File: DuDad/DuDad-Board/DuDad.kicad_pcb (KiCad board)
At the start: 2 copper layers, 60.6 x 24 mm, 24 parts, among them J1 EXP, J2 USB_B_Micro, J3 USB_A, Q1 2N3906, Q2 2N3906, Q3 2N7000, Q4 2N3906, SW1 Reset

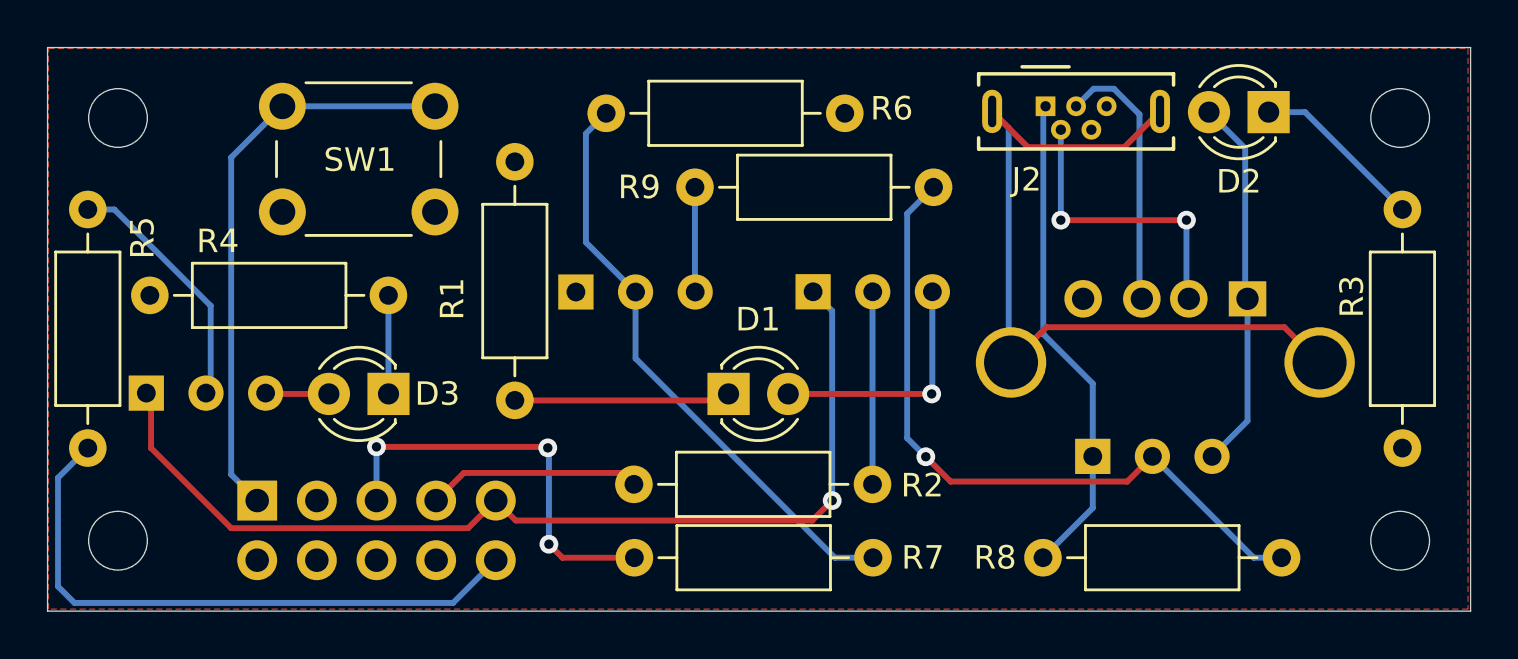
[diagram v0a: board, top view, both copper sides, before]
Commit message: Adds 2HP DuDad
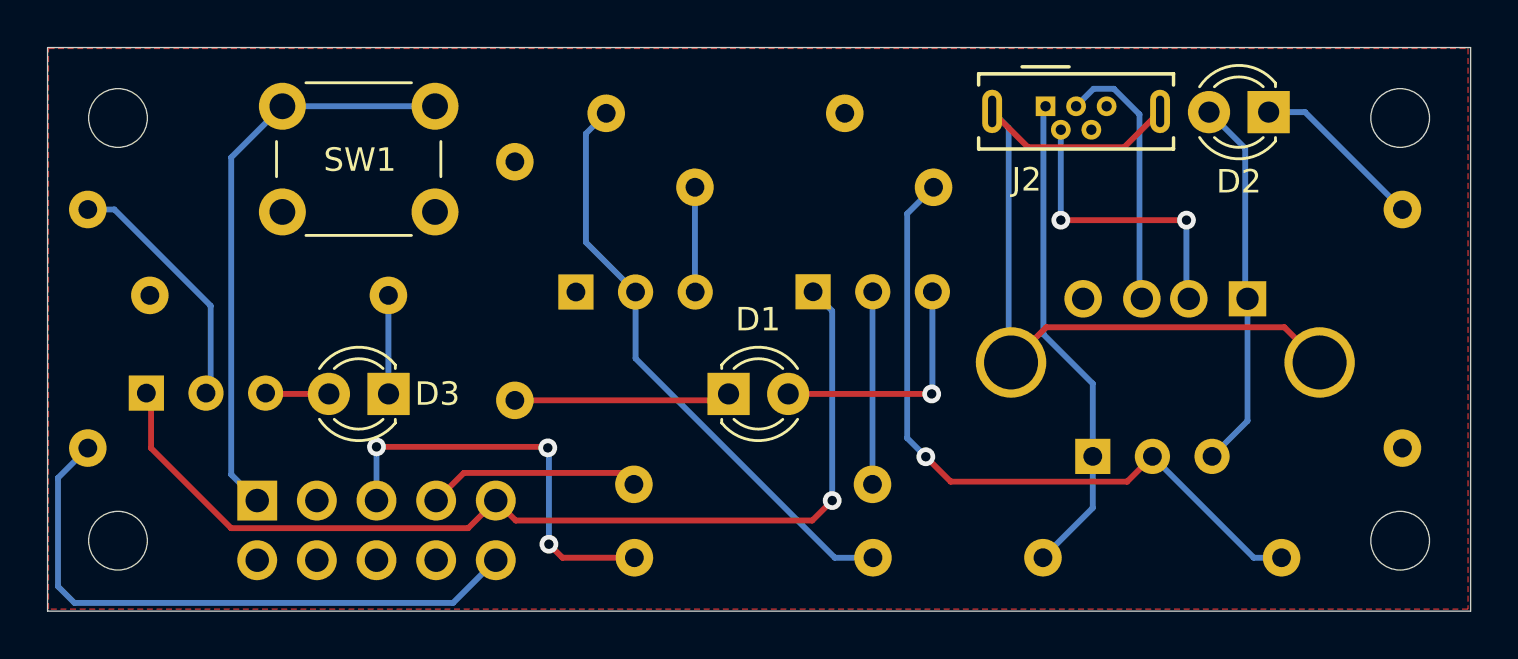
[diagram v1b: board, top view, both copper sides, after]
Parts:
- R1, R2, R3, R4, R5, R6, R7, R8, R9: moved to B.Cu
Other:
- board text added: "DuDad"
- board text added: "v1.4"
- board text removed: "DuDad v 1.3"

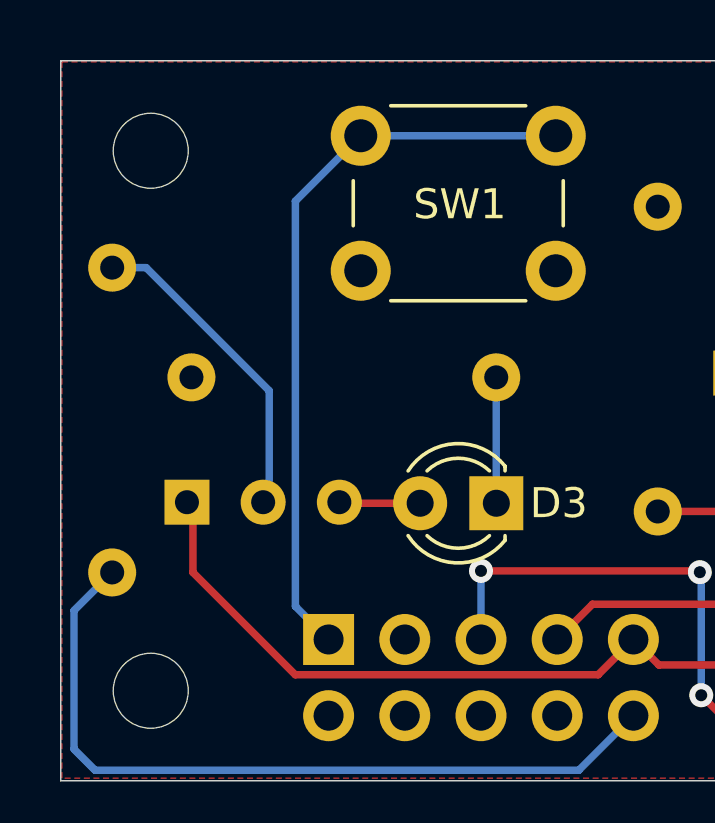
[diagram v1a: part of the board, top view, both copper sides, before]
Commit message: Ups resistor values to dim LEDs. Adds generate BOMs.
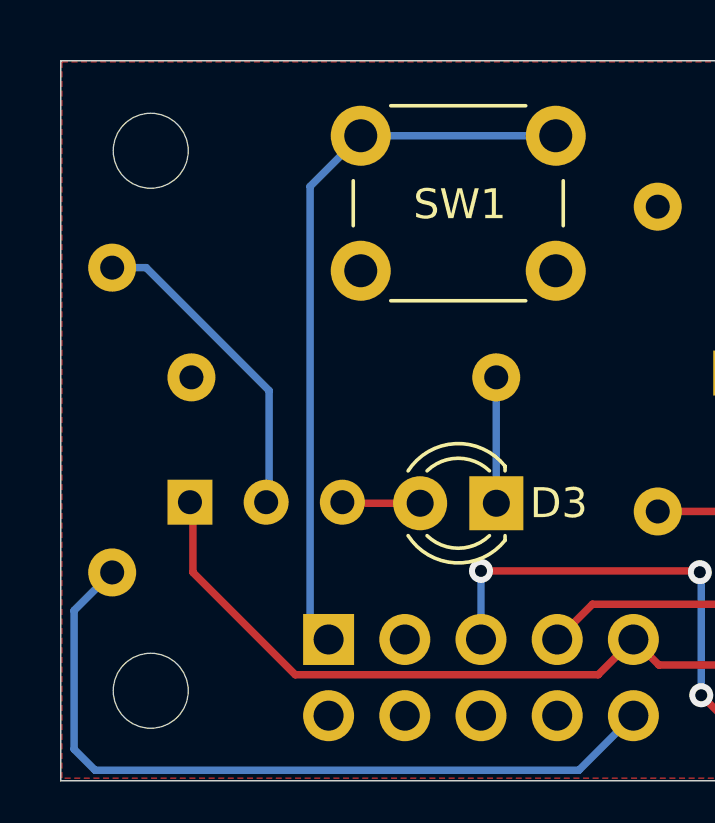
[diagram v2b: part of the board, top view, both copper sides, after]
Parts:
- R1, R4: value 200 -> 620
- R2, R5, R7, R8: value 43K -> 30K
- moved Q2 0.10 mm to (54.3, 64.7)
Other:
- board text added: "10K"
- board text added: "1K"
- board text added: "2N7000"
- board text added: "30K"
- board text added: "620"
- board text added: "v1.5"
- board text removed: "v1.4"
